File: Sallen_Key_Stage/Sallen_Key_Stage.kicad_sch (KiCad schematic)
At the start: 21 parts, among them J1 Conn_01x05_Pin, J2 Conn_01x05_Socket, U2 LM358

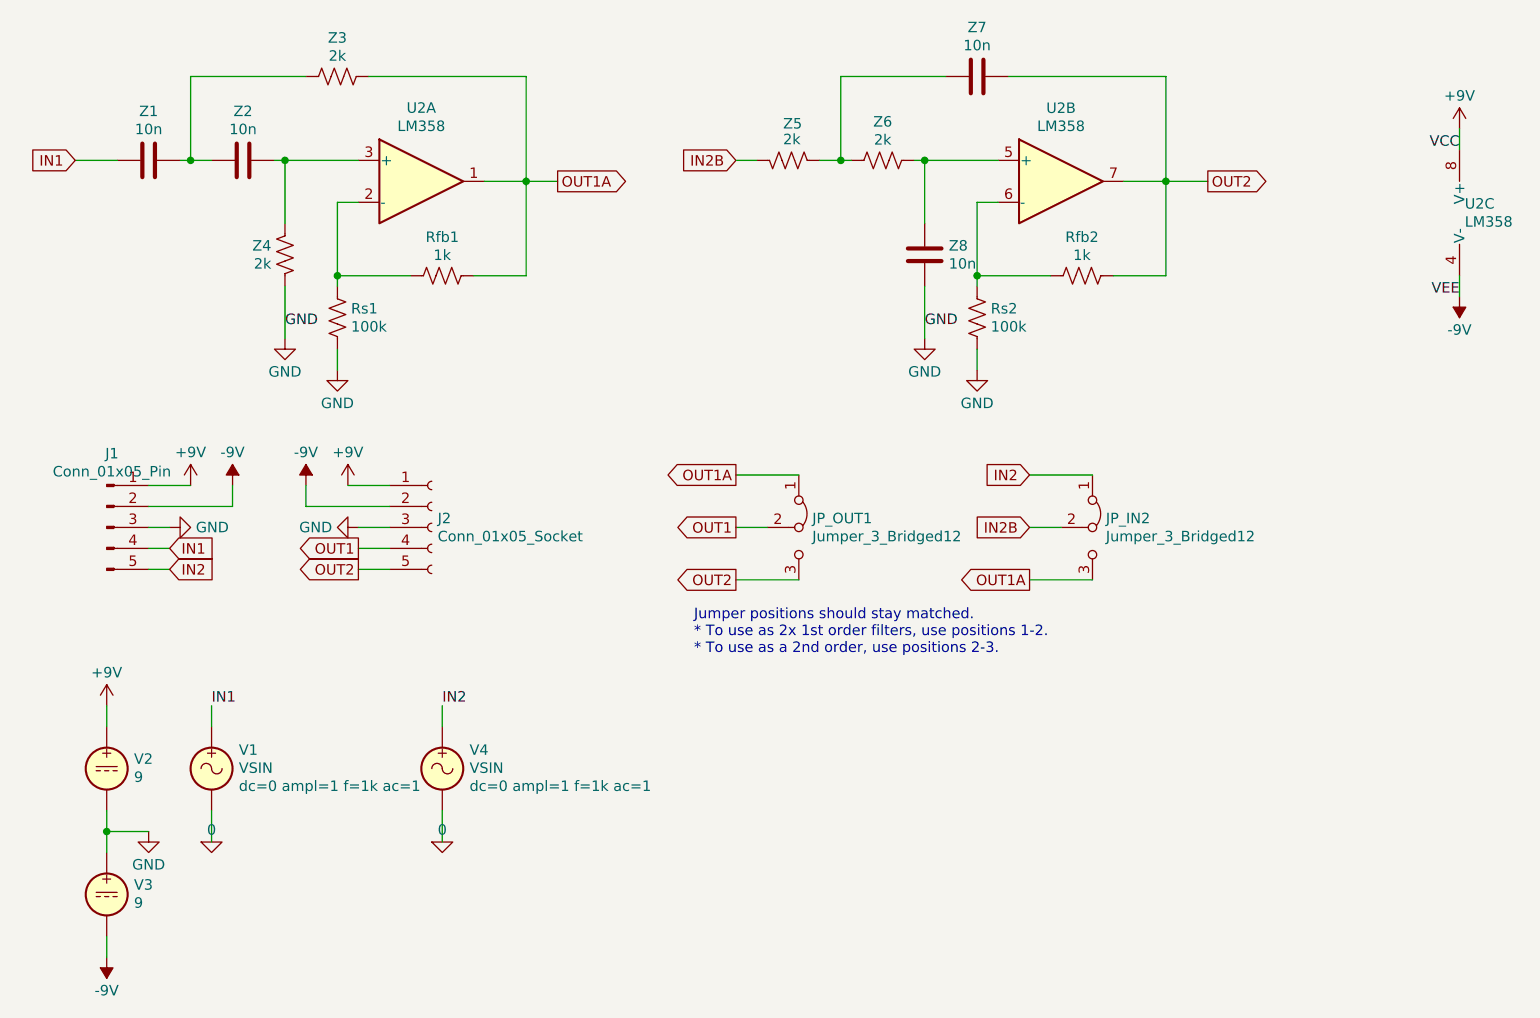
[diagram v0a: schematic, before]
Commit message: v1.0 of STLink-MIPI-14-to-SWD-10
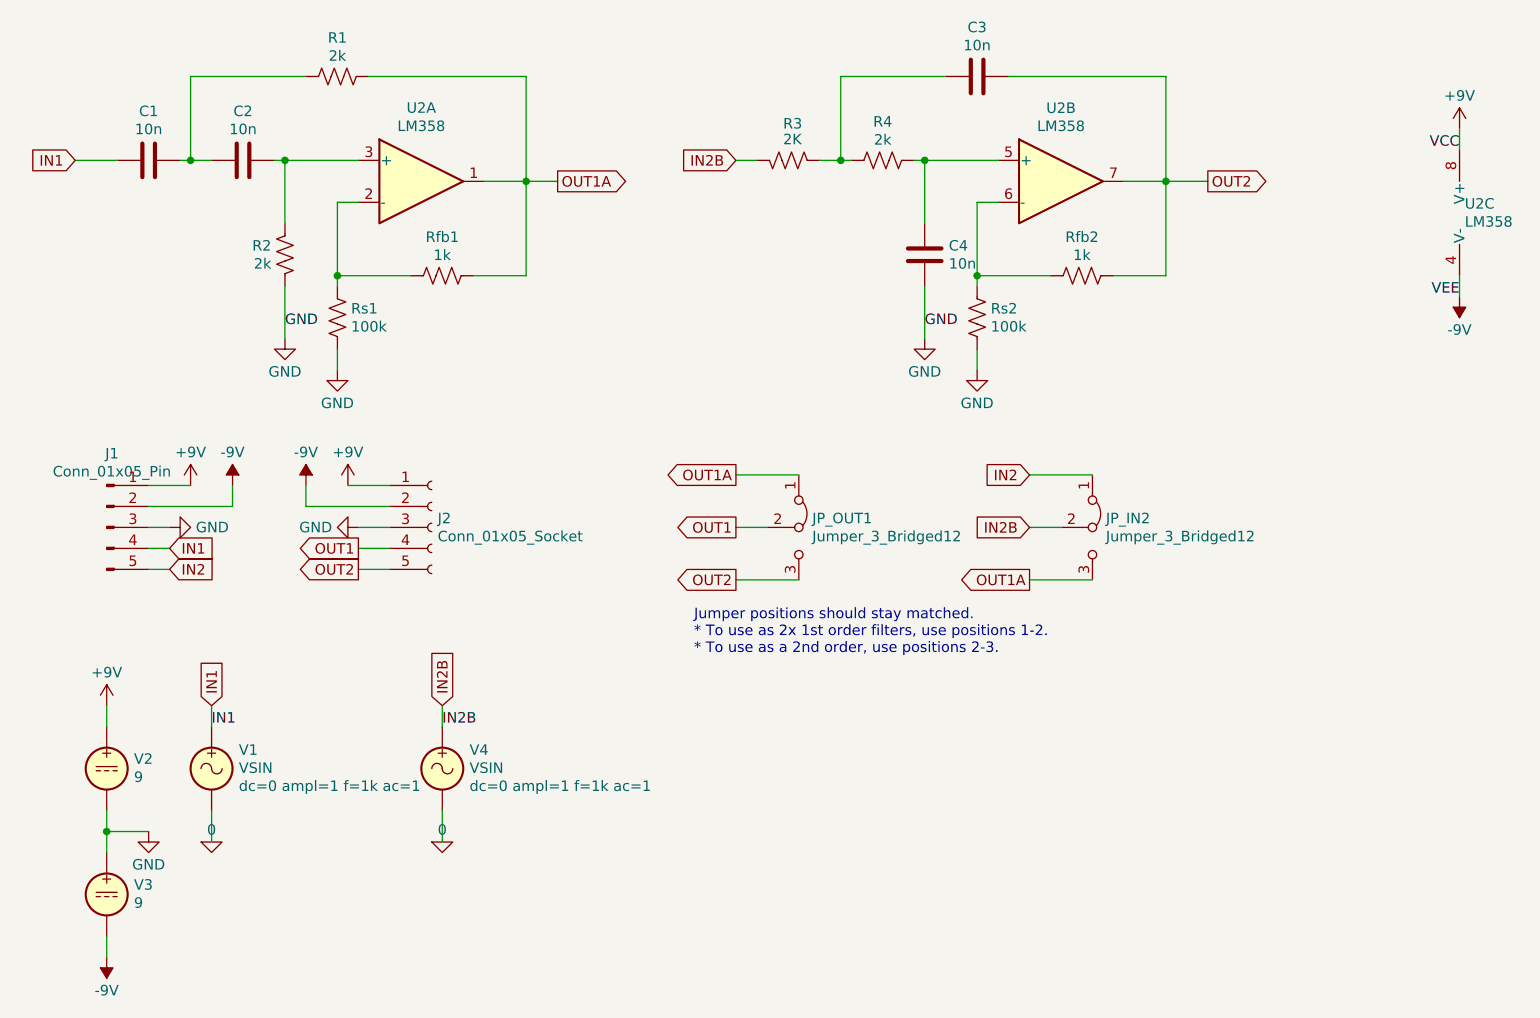
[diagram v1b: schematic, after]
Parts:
- R3: renamed from Z5; value 2k -> 2K
- U2: footprint Package_DIP:DIP-8_W7.62mm_Socket -> ProjectLibrary:PDIP_SOIC-8_3.9x4.9mm_P1.27mm
- renumbered Z1 to C1, Z2 to C2, Z7 to C3, Z8 to C4, Z3 to R1, Z4 to R2, Z6 to R4
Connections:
- net IN2: no longer V4.1
- net IN2B: now also V4.1
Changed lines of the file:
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@@
 	)
 	(label "IN1"
-		(at 38.1 97.79 0)
+		(at 38.1 100.33 0)
+		(fields_autoplaced yes)
+		(effects
+			(font
+				(size 1.27 1.27)
+			)
+			(justify left bottom)
+		)
+	)
+	(label "IN2B"
+		(at 66.04 100.33 0)
 		(fields_autoplaced yes)
 		(effects
@@
 		)
 	)
-	(label "IN2"
-		(at 66.04 97.79 0)
-		(fields_autoplaced yes)
-		(effects
-			(font
-				(size 1.27 1.27)
-			)
-			(justify left bottom)
-		)
-	)
 	(global_label "IN2"
 		(shape input)
@@
 		)
 	)
+	(global_label "IN1"
+		(shape input)
+		(at 38.1 97.79 90)
+		(fields_autoplaced yes)
+		(effects
+			(font
+				(size 1.27 1.27)
+			)
+			(justify left)
+		)
+		(property "Intersheetrefs" "${INTERSHEET_REFS}"
+			(at 38.1 92.0978 90)
+			(effects
+				(font
+					(size 1.27 1.27)
+				)
+				(justify left)
+				(hide yes)
+			)
+		)
+	)
 	(global_label "OUT1"
 		(shape output)
@@
 		)
 	)
+	(global_label "IN2B"
+		(shape input)
+		(at 66.04 97.79 90)
+		(fields_autoplaced yes)
+		(effects
+			(font
+				(size 1.27 1.27)
+			)
+			(justify left)
+		)
+		(property "Intersheetrefs" "${INTERSHEET_REFS}"
+			(at 66.04 91.1214 90)
+			(effects
+				(font
+					(size 1.27 1.27)
+				)
+				(justify left)
+				(hide yes)
+			)
+		)
+	)
 	(global_label "OUT2"
 		(shape output)
@@
 		(dnp no)
 		(fields_autoplaced yes)
-		(property "Reference" "Z6"
+		(property "Reference" "R4"
 			(at 119.38 27.0717 90)
 			(effects
@@
 			(project "Sallen_Key_Stage"
 				(path "/26487363-7305-4eb6-8afe-f50e7184f0af"
-					(reference "Z6")
+					(reference "R4")
 					(unit 1)
 				)
@@
 		(at 41.91 31.75 90)
 		(unit 1)
-		(exclude_from_sim no)
+		(exclude_from_sim yes)
 		(in_bom yes)
 		(on_board yes)
 		(dnp no)
 		(fields_autoplaced yes)
-		(property "Reference" "Z2"
+		(property "Reference" "C2"
 			(at 41.91 25.8017 90)
 			(effects
@@
 			)
 		)
+		(property "Sim.Device" "C"
+			(at 41.91 31.75 0)
+			(effects
+				(font
+					(size 1.27 1.27)
+				)
+				(hide yes)
+			)
+		)
+		(property "Sim.Pins" "1=+ 2=-"
+			(at 41.91 31.75 0)
+			(effects
+				(font
+					(size 1.27 1.27)
+				)
+				(hide yes)
+			)
+		)
+		(property "Sim.Params" "c=10n"
+			(at 41.91 31.75 0)
+			(effects
+				(font
+					(size 1.27 1.27)
+				)
+				(hide yes)
+			)
+		)
 		(pin "2"
 		)
@@
 			(project ""
 				(path "/26487363-7305-4eb6-8afe-f50e7184f0af"
-					(reference "Z2")
+					(reference "C2")
 					(unit 1)
 				)
@@
 		(at 140.97 34.29 0)
 		(unit 2)
-		(exclude_from_sim yes)
+		(exclude_from_sim no)
 		(in_bom yes)
 		(on_board yes)
@@
 			)
 		)
-		(property "Footprint" "Package_DIP:DIP-8_W7.62mm_Socket"
+		(property "Footprint" "ProjectLibrary:PDIP_SOIC-8_3.9x4.9mm_P1.27mm"
 			(at 140.97 34.29 0)
 			(effects
@@
 		(at 191.77 38.1 0)
 		(unit 3)
-		(exclude_from_sim yes)
+		(exclude_from_sim no)
 		(in_bom yes)
 		(on_board yes)
@@
 			)
 		)
-		(property "Footprint" "Package_DIP:DIP-8_W7.62mm_Socket"
+		(property "Footprint" "ProjectLibrary:PDIP_SOIC-8_3.9x4.9mm_P1.27mm"
 			(at 191.77 38.1 0)
 			(effects
@@
 			)
 		)
+		(property "Sim.Device" "R"
+			(at 109.22 76.2 0)
+			(effects
+				(font
+					(size 1.27 1.27)
+				)
+				(hide yes)
+			)
+		)
+		(property "Sim.Params" "r=1m"
+			(at 109.22 76.2 0)
+			(effects
+				(font
+					(size 1.27 1.27)
+				)
+				(hide yes)
+			)
+		)
+		(property "Sim.Pins" "1=+ 2=-"
+			(at 109.22 76.2 0)
+			(effects
+				(font
+					(size 1.27 1.27)
+				)
+				(hide yes)
+			)
+		)
 		(pin "1"
 		)
@@
 		(at 53.34 50.8 180)
 		(unit 1)
-		(exclude_from_sim no)
+		(exclude_from_sim yes)
 		(in_bom yes)
 		(on_board yes)
@@
 		(at 144.78 76.2 270)
 		(unit 1)
-		(exclude_from_sim yes)
+		(exclude_from_sim no)
 		(in_bom no)
 		(on_board yes)
@@
 			)
 		)
+		(property "Sim.Device" "R"
+			(at 144.78 76.2 0)
+			(effects
+				(font
+					(size 1.27 1.27)
+				)
+				(hide yes)
+			)
+		)
+		(property "Sim.Pins" "1=+ 2=-"
+			(at 144.78 76.2 0)
+			(effects
+				(font
+					(size 1.27 1.27)
+				)
+				(hide yes)
+			)
+		)
+		(property "Sim.Params" "r=1m"
+			(at 144.78 76.2 0)
+			(effects
+				(font
+					(size 1.27 1.27)
+				)
+				(hide yes)
+			)
+		)
 		(pin "1"
 		)
@@
 		(dnp no)
 		(fields_autoplaced yes)
-		(property "Reference" "Z8"
+		(property "Reference" "C4"
 			(at 127.381 42.0862 0)
 			(effects
@@
 			)
 		)
+		(property "Sim.Device" "C"
+			(at 124.46 43.18 0)
+			(effects
+				(font
+					(size 1.27 1.27)
+				)
+				(hide yes)
+			)
+		)
+		(property "Sim.Pins" "1=+ 2=-"
+			(at 124.46 43.18 0)
+			(effects
+				(font
+					(size 1.27 1.27)
+				)
+				(hide yes)
+			)
+		)
+		(property "Sim.Params" "c=10n"
+			(at 124.46 43.18 0)
+			(effects
+				(font
+					(size 1.27 1.27)
+				)
+				(hide yes)
+			)
+		)
 		(pin "2"
 		)
@@
 			(project "Sallen_Key_Stage"
 				(path "/26487363-7305-4eb6-8afe-f50e7184f0af"
-					(reference "Z8")
+					(reference "C4")
 					(unit 1)
 				)
@@
 		(mirror y)
 		(unit 1)
-		(exclude_from_sim no)
+		(exclude_from_sim yes)
 		(in_bom yes)
 		(on_board yes)
 		(dnp no)
-		(property "Reference" "Z4"
+		(property "Reference" "R2"
 			(at 45.339 42.0862 0)
 			(effects
@@
 			(project ""
 				(path "/26487363-7305-4eb6-8afe-f50e7184f0af"
-					(reference "Z4")
+					(reference "R2")
 					(unit 1)
 				)
@@
 		(at 53.34 21.59 90)
 		(unit 1)
-		(exclude_from_sim no)
+		(exclude_from_sim yes)
 		(in_bom yes)
 		(on_board yes)
 		(dnp no)
 		(fields_autoplaced yes)
-		(property "Reference" "Z3"
+		(property "Reference" "R1"
 			(at 53.34 16.9117 90)
 			(effects
@@
 			(project ""
 				(path "/26487363-7305-4eb6-8afe-f50e7184f0af"
-					(reference "Z3")
+					(reference "R1")
 					(unit 1)
 				)
@@
 		(at 30.48 31.75 90)
 		(unit 1)
-		(exclude_from_sim no)
+		(exclude_from_sim yes)
 		(in_bom yes)
 		(on_board yes)
 		(dnp no)
 		(fields_autoplaced yes)
-		(property "Reference" "Z1"
+		(property "Reference" "C1"
 			(at 30.48 25.8017 90)
 			(effects
@@
 			(project ""
 				(path "/26487363-7305-4eb6-8afe-f50e7184f0af"
-					(reference "Z1")
+					(reference "C1")
 					(unit 1)
 				)
@@
 		(at 63.5 34.29 0)
 		(unit 1)
-		(exclude_from_sim yes)
+		(exclude_from_sim no)
 		(in_bom yes)
 		(on_board yes)
@@
 			)
 		)
-		(property "Footprint" "Package_DIP:DIP-8_W7.62mm_Socket"
+		(property "Footprint" "ProjectLibrary:PDIP_SOIC-8_3.9x4.9mm_P1.27mm"
 			(at 63.5 34.29 0)
 			(effects
@@
 		(at 66.04 45.72 90)
 		(unit 1)
-		(exclude_from_sim no)
+		(exclude_from_sim yes)
 		(in_bom yes)
 		(on_board yes)
@@
 			)
 		)
+		(property "Sim.Device" "R"
+			(at 66.04 45.72 0)
+			(effects
+				(font
+					(size 1.27 1.27)
+				)
+				(hide yes)
+			)
+		)
+		(property "Sim.Pins" "1=+ 2=-"
+			(at 66.04 45.72 0)
+			(effects
+				(font
+					(size 1.27 1.27)
+				)
+				(hide yes)
+			)
+		)
 		(pin "1"
 		)
@@
 		(on_board yes)
 		(dnp no)
-		(property "Reference" "Z5"
+		(property "Reference" "R3"
 			(at 107.315 27.305 90)
 			(effects
@@
 			)
 		)
-		(property "Value" "2k"
+		(property "Value" "2K"
 			(at 107.315 29.21 90)
 			(effects
@@
 			(project "Sallen_Key_Stage"
 				(path "/26487363-7305-4eb6-8afe-f50e7184f0af"
-					(reference "Z5")
+					(reference "R3")
 					(unit 1)
 				)
@@
 		(dnp no)
 		(fields_autoplaced yes)
-		(property "Reference" "Z7"
+		(property "Reference" "C3"
 			(at 130.81 15.6417 90)
 			(effects
@@
 			(project "Sallen_Key_Stage"
 				(path "/26487363-7305-4eb6-8afe-f50e7184f0af"
-					(reference "Z7")
+					(reference "C3")
 					(unit 1)
 				)
@@
 		(at 64.77 76.2 0)
 		(unit 1)
-		(exclude_from_sim no)
+		(exclude_from_sim yes)
 		(in_bom yes)
 		(on_board yes)
@@
 		(at 25.4 76.2 0)
 		(unit 1)
-		(exclude_from_sim no)
+		(exclude_from_sim yes)
 		(in_bom yes)
 		(on_board yes)
